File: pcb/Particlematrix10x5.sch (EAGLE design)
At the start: 65 parts

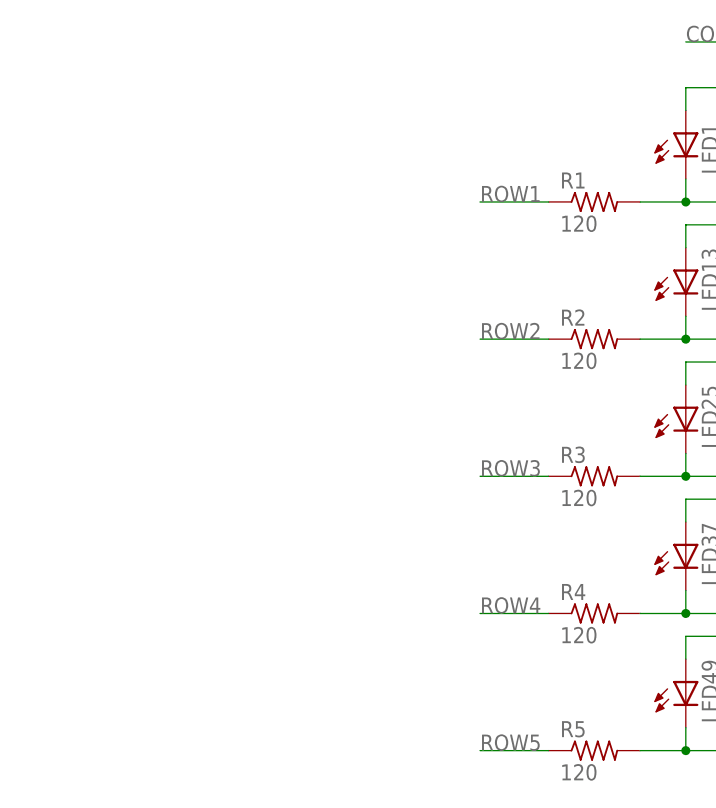
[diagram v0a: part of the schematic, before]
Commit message: Added 4017 decade counter to schematic
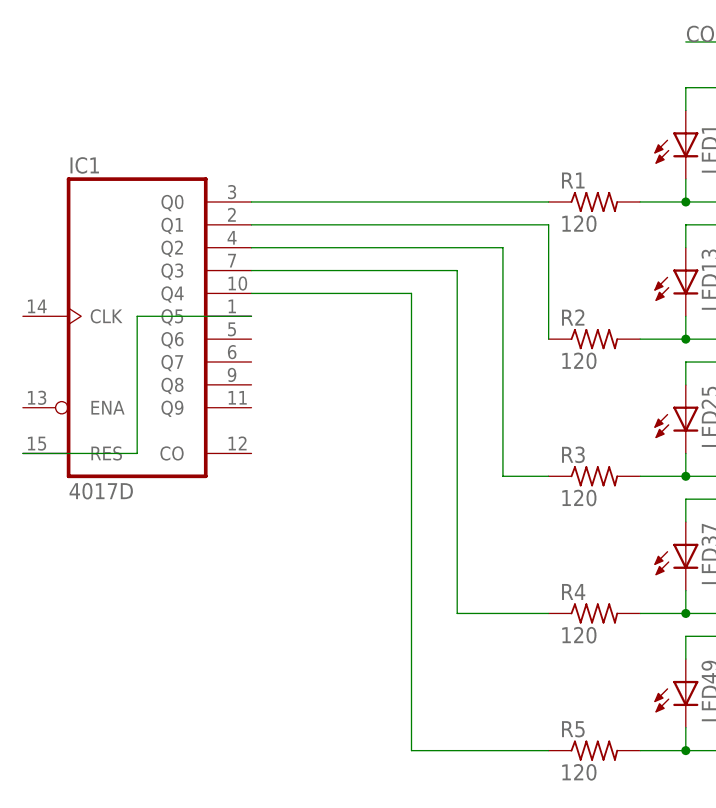
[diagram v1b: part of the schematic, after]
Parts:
- added IC1: 4017D, 40xx:4017D
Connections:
- removed net ROW1: R1.1
- removed net ROW2: R2.1
- removed net ROW3: R3.1
- removed net ROW4: R4.1
- removed net ROW5: R5.1
- new net N$1: IC1A.Q0, R1.1
- new net N$2: IC1A.Q1, R2.1
- new net N$3: IC1A.Q2, R3.1
- new net N$4: IC1A.Q3, R4.1
- new net N$5: IC1A.Q4, R5.1
- new net N$6: IC1A.Q5, IC1A.RES
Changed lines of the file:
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@@
 <part name="LED48" library="adafruit" deviceset="LED" device="5MM"/>
 <part name="LED60" library="adafruit" deviceset="LED" device="5MM"/>
+<part name="IC1" library="40xx" deviceset="4017" device="D"/>
 </parts>
 <sheets>
@@
 <instance part="LED48" gate="G$1" x="231.14" y="88.9"/>
 <instance part="LED60" gate="G$1" x="231.14" y="73.66"/>
+<instance part="IC1" gate="A" x="58.42" y="114.3"/>
 </instances>
 <busses>
@@
 <pinref part="LED39" gate="G$1" pin="A"/>
 <pinref part="LED51" gate="G$1" pin="A"/>
-</segment>
-</net>
-<net name="ROW1" class="0">
-<segment>
-<pinref part="R1" gate="G$1" pin="1"/>
-<label x="96.52" y="127" size="1.778" layer="95"/>
-<wire x1="104.14" y1="127" x2="96.52" y2="127" width="0.1524" layer="91"/>
 </segment>
 </net>
@@
 </segment>
 </net>
-<net name="ROW2" class="0">
-<segment>
-<pinref part="R2" gate="G$1" pin="1"/>
-<wire x1="104.14" y1="111.76" x2="96.52" y2="111.76" width="0.1524" layer="91"/>
-<label x="96.52" y="111.76" size="1.778" layer="95"/>
-</segment>
-</net>
-<net name="ROW3" class="0">
-<segment>
-<pinref part="R3" gate="G$1" pin="1"/>
-<wire x1="104.14" y1="96.52" x2="96.52" y2="96.52" width="0.1524" layer="91"/>
-<label x="96.52" y="96.52" size="1.778" layer="95"/>
-</segment>
-</net>
-<net name="ROW4" class="0">
-<segment>
-<pinref part="R4" gate="G$1" pin="1"/>
-<wire x1="104.14" y1="81.28" x2="96.52" y2="81.28" width="0.1524" layer="91"/>
-<label x="96.52" y="81.28" size="1.778" layer="95"/>
-</segment>
-</net>
 <net name="$9" class="0">
 <segment>
@@
 </segment>
 </net>
-<net name="ROW5" class="0">
-<segment>
-<pinref part="R5" gate="G$1" pin="1"/>
-<wire x1="104.14" y1="66.04" x2="96.52" y2="66.04" width="0.1524" layer="91"/>
-<label x="96.52" y="66.04" size="1.778" layer="95"/>
-</segment>
-</net>
 <net name="COL5" class="0">
 <segment>
@@
 </segment>
 </net>
+<net name="N$1" class="0">
+<segment>
+<pinref part="IC1" gate="A" pin="Q0"/>
+<pinref part="R1" gate="G$1" pin="1"/>
+<wire x1="71.12" y1="127" x2="104.14" y2="127" width="0.1524" layer="91"/>
+</segment>
+</net>
+<net name="N$2" class="0">
+<segment>
+<pinref part="IC1" gate="A" pin="Q1"/>
+<pinref part="R2" gate="G$1" pin="1"/>
+<wire x1="71.12" y1="124.46" x2="104.14" y2="124.46" width="0.1524" layer="91"/>
+<wire x1="104.14" y1="124.46" x2="104.14" y2="111.76" width="0.1524" layer="91"/>
+</segment>
+</net>
+<net name="N$3" class="0">
+<segment>
+<pinref part="IC1" gate="A" pin="Q2"/>
+<wire x1="71.12" y1="121.92" x2="99.06" y2="121.92" width="0.1524" layer="91"/>
+<wire x1="99.06" y1="121.92" x2="99.06" y2="96.52" width="0.1524" layer="91"/>
+<pinref part="R3" gate="G$1" pin="1"/>
+<wire x1="99.06" y1="96.52" x2="104.14" y2="96.52" width="0.1524" layer="91"/>
+</segment>
+</net>
+<net name="N$4" class="0">
+<segment>
+<pinref part="IC1" gate="A" pin="Q3"/>
+<wire x1="71.12" y1="119.38" x2="93.98" y2="119.38" width="0.1524" layer="91"/>
+<wire x1="93.98" y1="119.38" x2="93.98" y2="81.28" width="0.1524" layer="91"/>
+<pinref part="R4" gate="G$1" pin="1"/>
+<wire x1="93.98" y1="81.28" x2="104.14" y2="81.28" width="0.1524" layer="91"/>
+</segment>
+</net>
+<net name="N$5" class="0">
+<segment>
+<pinref part="IC1" gate="A" pin="Q4"/>
+<wire x1="71.12" y1="116.84" x2="88.9" y2="116.84" width="0.1524" layer="91"/>
+<wire x1="88.9" y1="116.84" x2="88.9" y2="66.04" width="0.1524" layer="91"/>
+<pinref part="R5" gate="G$1" pin="1"/>
+<wire x1="88.9" y1="66.04" x2="104.14" y2="66.04" width="0.1524" layer="91"/>
+</segment>
+</net>
+<net name="N$6" class="0">
+<segment>
+<pinref part="IC1" gate="A" pin="Q5"/>
+<wire x1="71.12" y1="114.3" x2="58.42" y2="114.3" width="0.1524" layer="91"/>
+<wire x1="58.42" y1="114.3" x2="58.42" y2="99.06" width="0.1524" layer="91"/>
+<pinref part="IC1" gate="A" pin="RES"/>
+<wire x1="58.42" y1="99.06" x2="45.72" y2="99.06" width="0.1524" layer="91"/>
+</segment>
+</net>

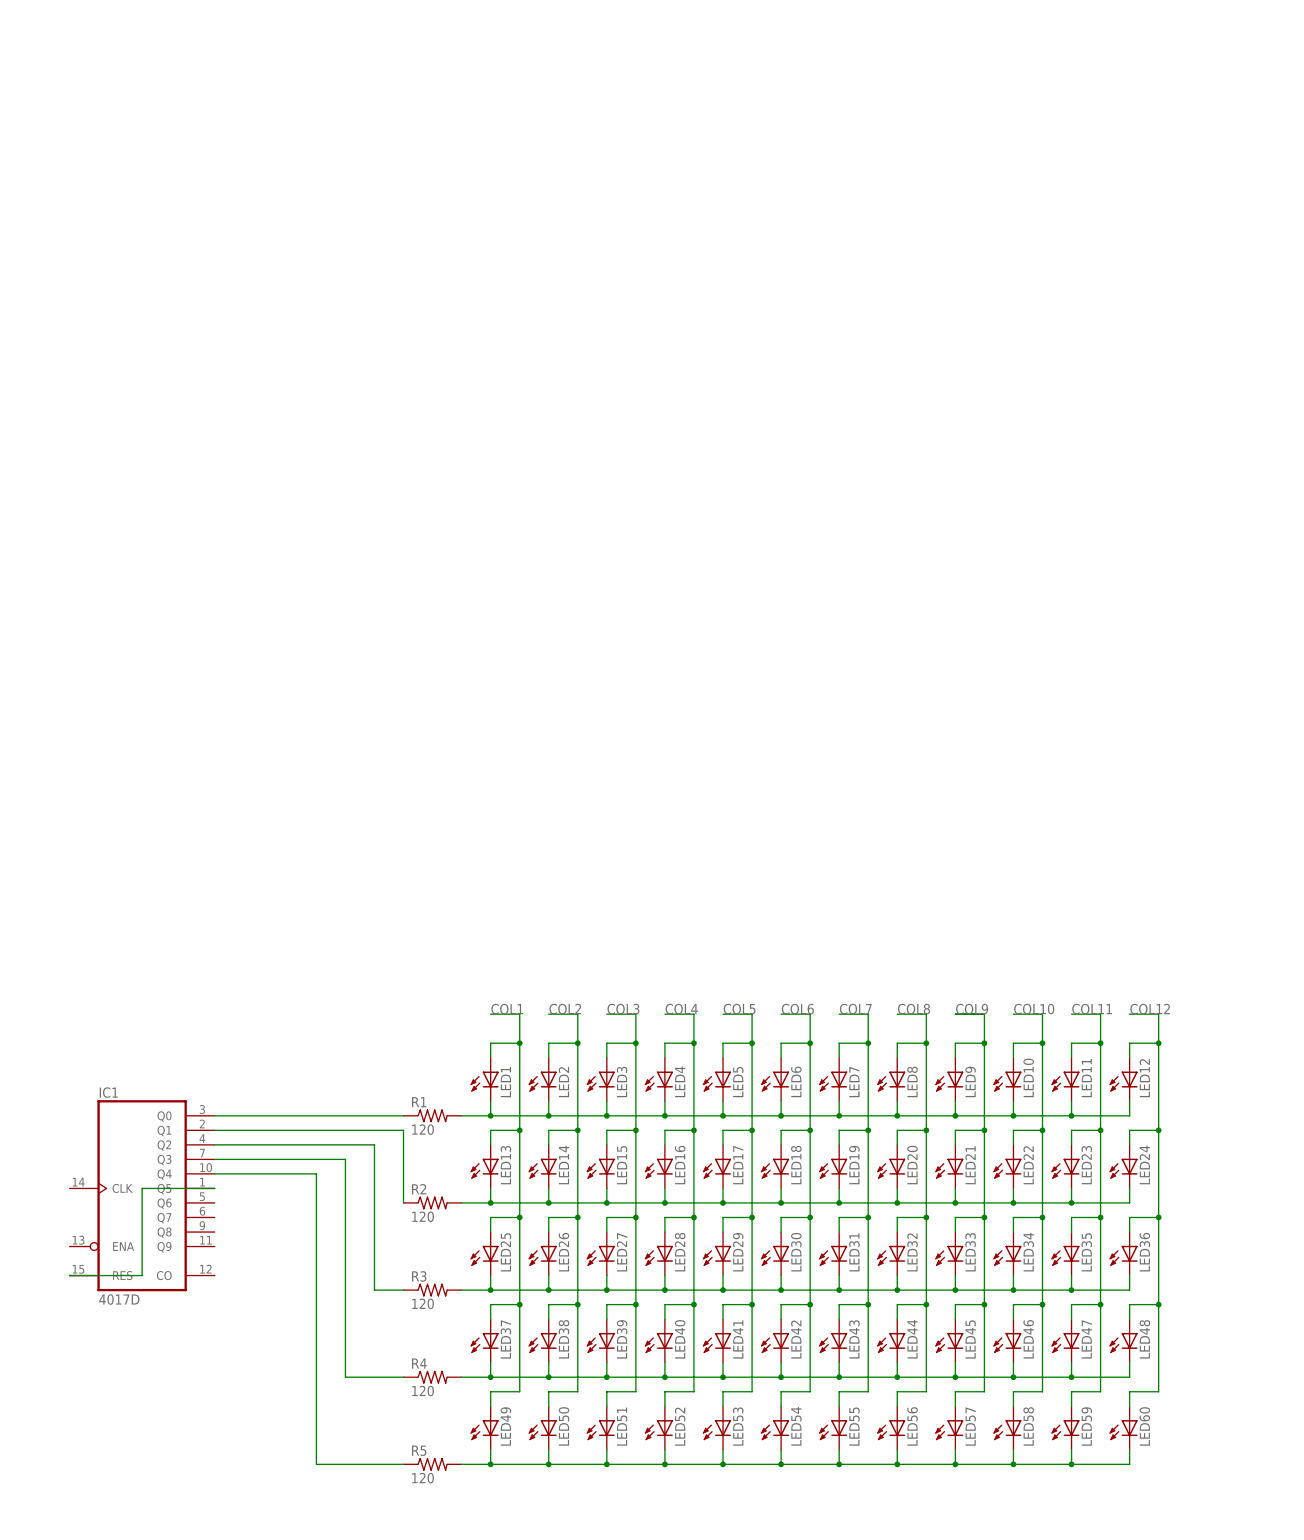
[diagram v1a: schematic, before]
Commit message: Routed all LEDs, decade counter, and Arduino Mega
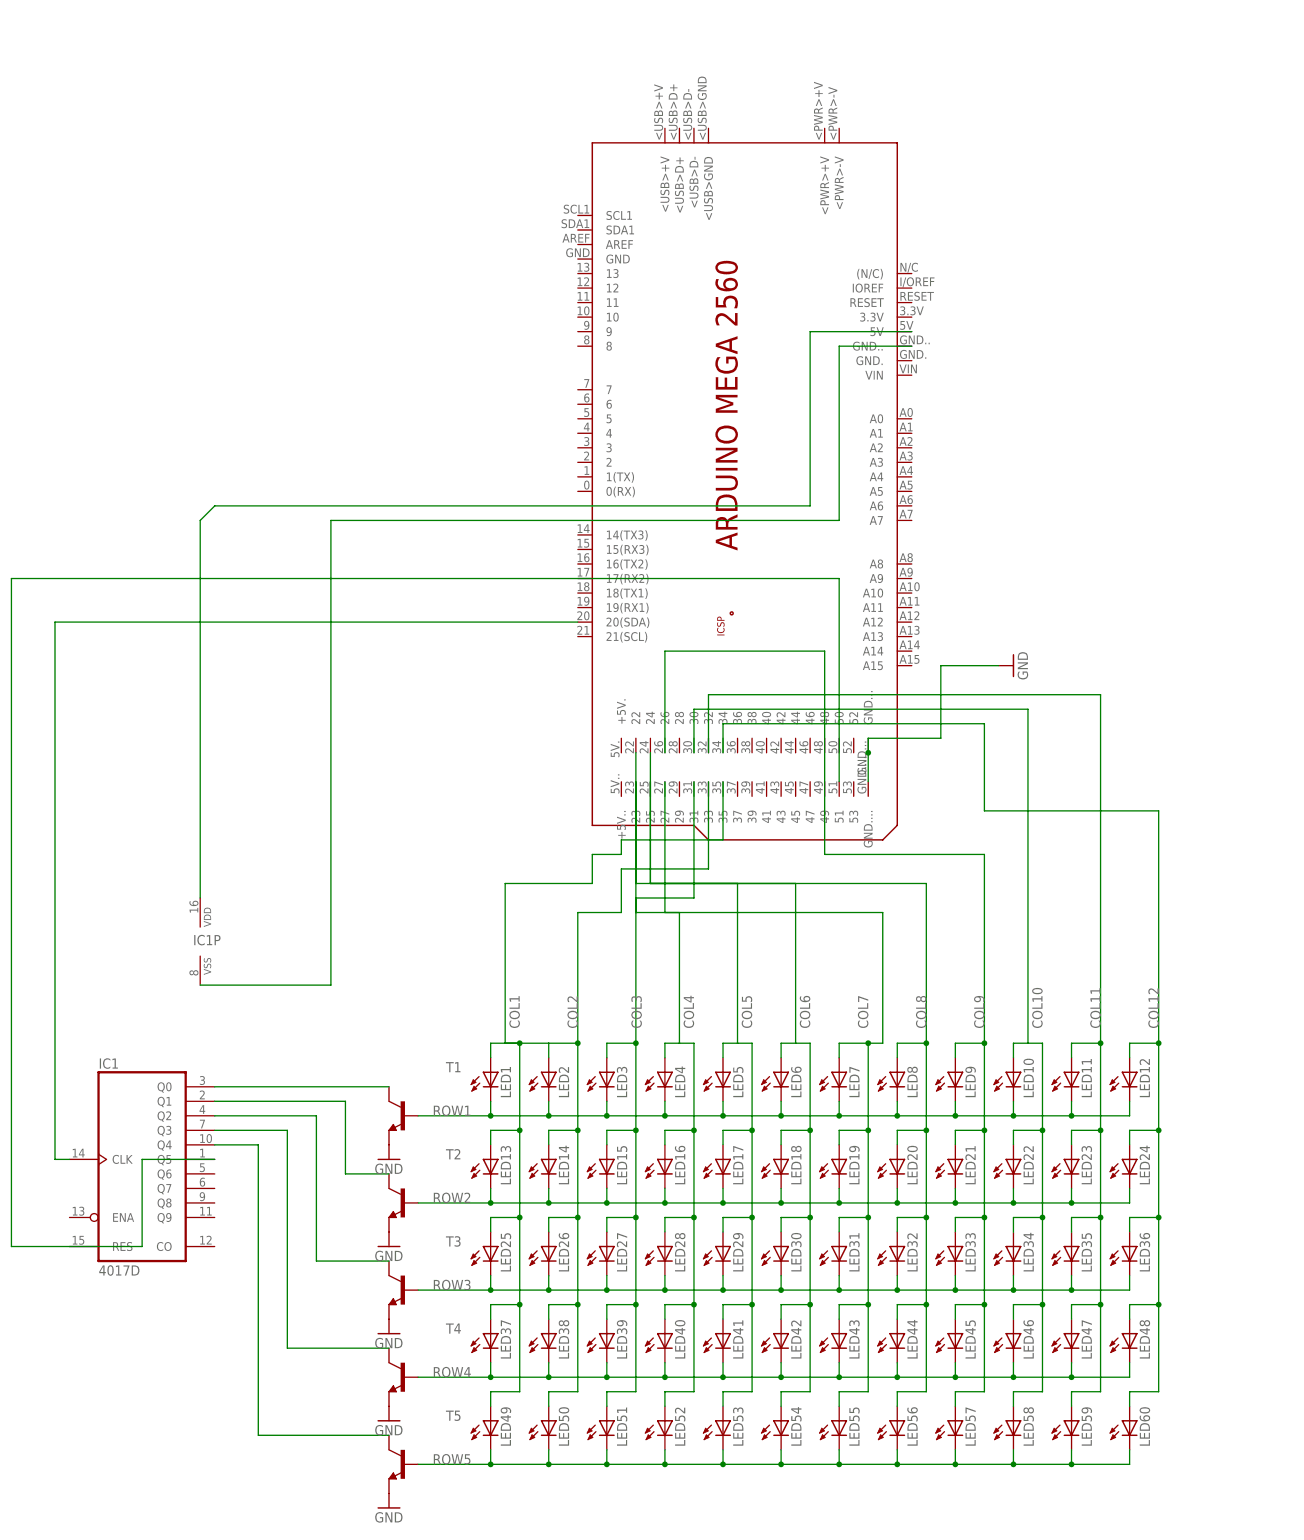
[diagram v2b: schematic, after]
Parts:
- removed R1, R2, R3, R4, R5: 120, resistor:R-US_M0805
- added PCB1: ARDUINO_MEGA2560, E14_Arduino_revB:ARDUINO_MEGA2560
- added T1, T2, T3, T4, T5: (no value), transistor-neu-to92:2N3904-NPN-TO92-EBC
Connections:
- removed net $1: LED1.C, LED10.C, LED11.C, LED12.C, LED2.C, LED3.C, LED4.C, LED5.C, LED6.C, LED7.C, LED8.C, LED9.C, R1.2
- removed net $2: LED13.C, LED14.C, LED15.C, LED16.C, LED17.C, LED18.C, LED19.C, LED20.C, LED21.C, LED22.C, LED23.C, LED24.C, R2.2
- removed net $3: LED25.C, LED26.C, LED27.C, LED28.C, LED29.C, LED30.C, LED31.C, LED32.C, LED33.C, LED34.C, LED35.C, LED36.C, R3.2
- removed net $4: LED37.C, LED38.C, LED39.C, LED40.C, LED41.C, LED42.C, LED43.C, LED44.C, LED45.C, LED46.C, LED47.C, LED48.C, R4.2
- removed net $9: LED49.C, LED50.C, LED51.C, LED52.C, LED53.C, LED54.C, LED55.C, LED56.C, LED57.C, LED58.C, LED59.C, LED60.C, R5.2
- new net GND: PCB1.GND..., PCB1.GND...., T1.E, T2.E, T3.E, T4.E, T5.E
- new net N$7: IC1A.CLK, PCB1.20(SDA)
- new net N$8: IC1A.Q5, IC1A.RES, PCB1.51
- new net N$9: IC1P.VSS, PCB1.GND..
- new net ROW1: LED1.C, LED10.C, LED11.C, LED12.C, LED2.C, LED3.C, LED4.C, LED5.C, LED6.C, LED7.C, LED8.C, LED9.C, T1.B
- new net ROW2: LED13.C, LED14.C, LED15.C, LED16.C, LED17.C, LED18.C, LED19.C, LED20.C, LED21.C, LED22.C, LED23.C, LED24.C, T2.B
- new net ROW3: LED25.C, LED26.C, LED27.C, LED28.C, LED29.C, LED30.C, LED31.C, LED32.C, LED33.C, LED34.C, LED35.C, LED36.C, T3.B
- new net ROW4: LED37.C, LED38.C, LED39.C, LED40.C, LED41.C, LED42.C, LED43.C, LED44.C, LED45.C, LED46.C, LED47.C, LED48.C, T4.B
- new net ROW5: LED49.C, LED50.C, LED51.C, LED52.C, LED53.C, LED54.C, LED55.C, LED56.C, LED57.C, LED58.C, LED59.C, LED60.C, T5.B
- net COL1: now also PCB1.35
- net COL10: now also PCB1.30
- net COL11: now also PCB1.32
- net COL12: now also PCB1.34
- net COL2: now also PCB1.33
- net COL3: now also PCB1.31
- net COL4: now also PCB1.27
- net COL5: now also PCB1.25
- net COL6: now also PCB1.23
- net COL7: now also PCB1.22
- net COL8: now also PCB1.24
- net COL9: now also PCB1.26
- net N$1: now also T1.C; no longer R1.1
- net N$2: now also T2.C; no longer R2.1
- net N$3: now also T3.C; no longer R3.1
- net N$4: now also T4.C; no longer R4.1
- net N$5: now also T5.C; no longer R5.1
- net N$6: now also IC1P.VDD, PCB1.5V; no longer IC1A.Q5, IC1A.RES
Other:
- moved on the sheet: IC1
